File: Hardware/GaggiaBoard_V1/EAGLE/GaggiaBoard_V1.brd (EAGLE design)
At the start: 80 x 100 mm, 85 parts, among them IC1 LD117ADT33TR, J2 Vertical Qwiic Connector, J3 Vertical Qwiic Connector, J4 1X2-3.5MM, J5 1X2-3.5MM, K1 RELAY-SPDT-JZC-11F, K2 RELAY-SPDT-JZC-11F, K3 RELAY-SPDT-JZC-11F, Q1 600mA/40V, Q2 600mA/40V, Q3 600mA/40V, Q4 600mA/40V, Q5 600mA/40V, Q6 600mA/40V, Q7 2N7002D, Q8 600mA/40V, Q9 600mA/40V, U1 BLACKPILL, U2 MAX31855K, U3 MAX31855K, U4 MOC3021MDIL06O

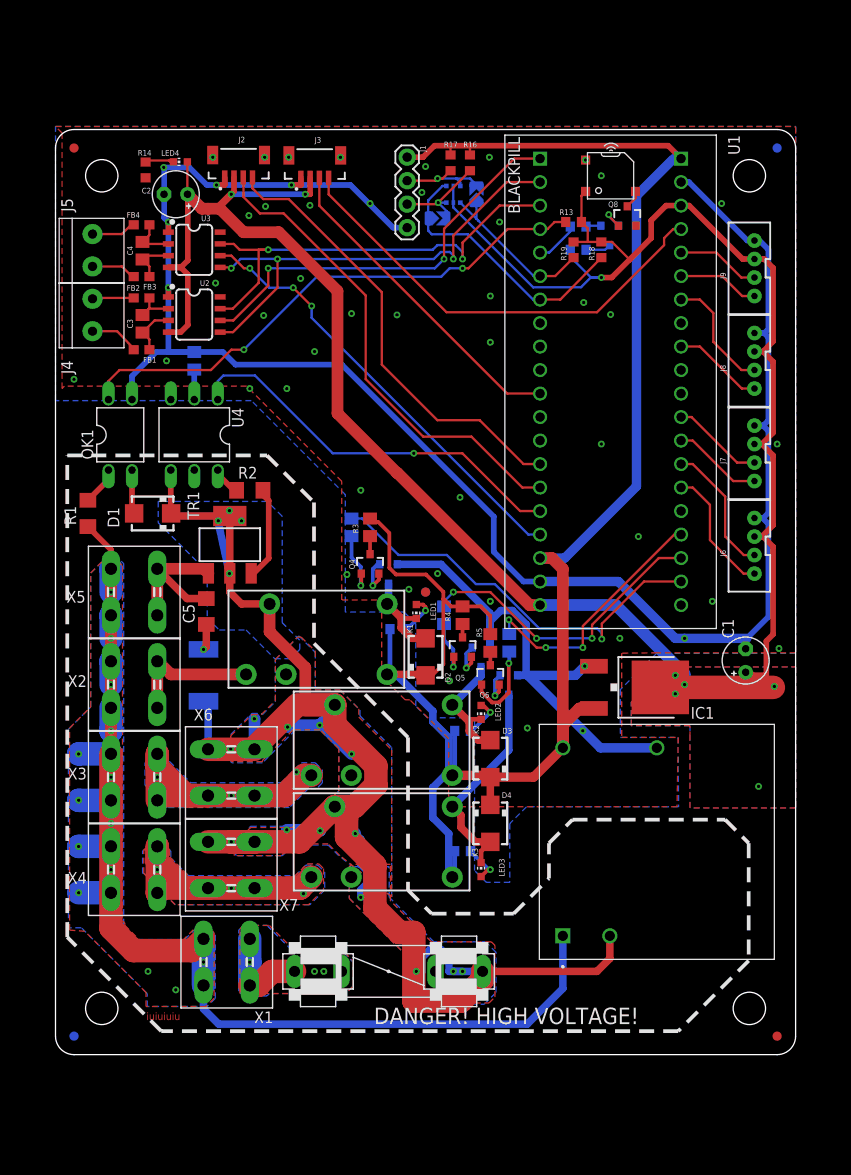
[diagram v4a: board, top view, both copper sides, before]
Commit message: PSU replaced
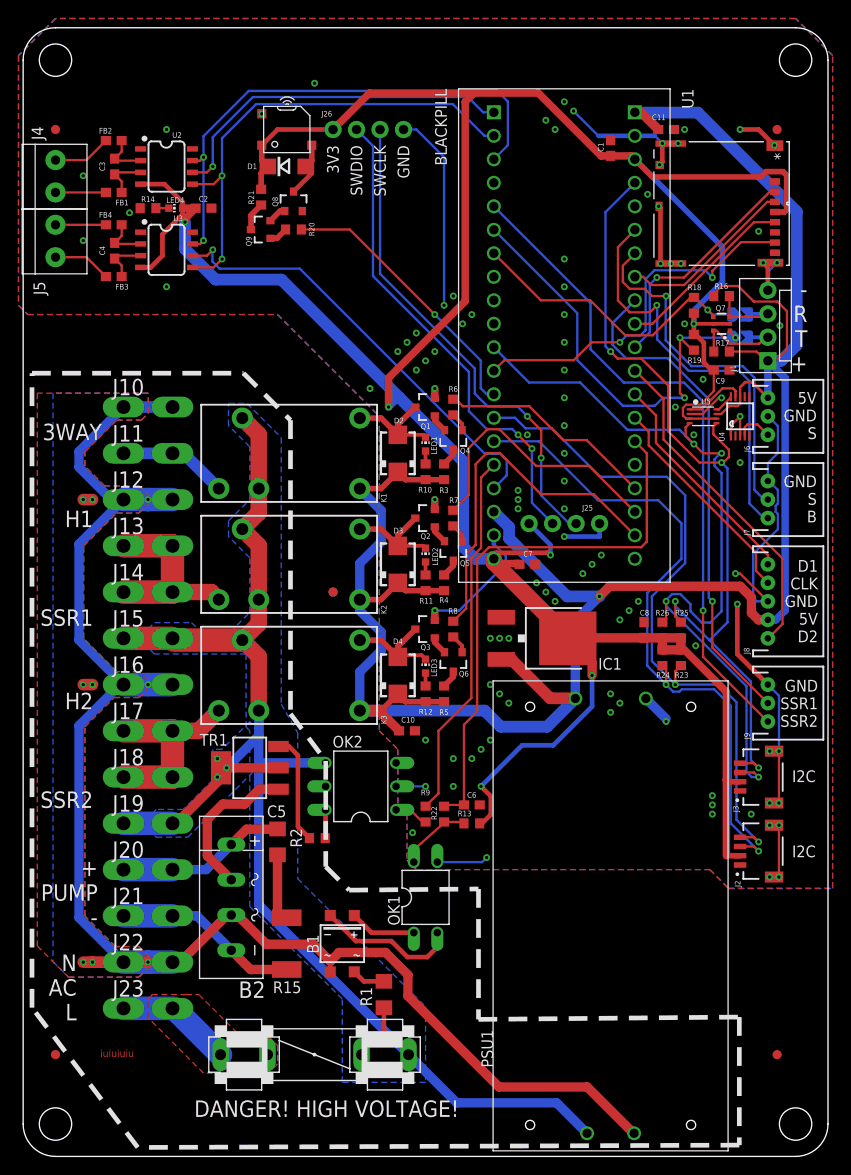
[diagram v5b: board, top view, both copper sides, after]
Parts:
- removed PS1: PSK-3D-5, PSK-3D-5:CONV_PSK-3D-5
- removed X1, X2, X3, X4, X5, X6, X7: (no value), con-rib:SH5-2
- added B1: MB6S, rectifier:SOIC-4
- added B2: RECTIFIER-2KBP, rectifier:2KBP
- added C10, C11, C6, C7, C8, C9: 10uF/16V, rcl:C0603
- added J10, J11, J12, J13, J14, J15, J16, J17, J18, J19, J20, J21, J22, J23: PIN262409-1, con-faston:62409-1
- added J24: 5033981892, discrete:503398-1892_MOL
- added J25, J26: (no value), SparkFun-Connectors:1X04_NO_SILK
- added OK2: MOC3021MDIL06O, discrete:DIL06O
- added PSU1: SM-PLG06-05, discrete:SM-PLG06
- added R22: 100, rcl:R0603
- added R23, R24, R25, R26: 10K, rcl:R0603
- added U5: (no value), adafruit:VFSOP-8
- C1, C2: device rcl:E2,5-5 -> rcl:C0603
- C3, C4: device rcl:C0805 -> rcl:C0603
- D1: value S1M -> 1N4007; device diode:SMA -> diode:DO214AC
- F1: value 30A -> 6A
- J1: device SparkFun-Connectors:1X04 -> SparkFun-Connectors:MOLEX-1X4
- J2, J3: value Vertical Qwiic Connector -> QWIIC_RIGHT_ANGLE; device SparkFun-Connectors:JST04_1MM_VERT -> SparkFun-Connectors:JST04_1MM_RA
- J6, J7, J9: device SparkFun-Connectors:JST-4-PTH-VERT -> SparkFun-Connectors:JST-3-PTH
- J8: device SparkFun-Connectors:JST-4-PTH-VERT -> SparkFun-Connectors:JST-5-PTH
- Q7: value 2N7002D -> (none)
- R10, R11, R12: value 330 -> 120
- R14: value 330 -> 51
- R2: device rcl:R1206 -> rcl:R0603
- R3, R4, R5, R6, R7, R8, R9: device rcl:R0805 -> rcl:R0603
- U4: value MOC3021MDIL06O -> (none); device discrete:DIL06O -> microbuilder:MSOP10
- moved J2 90.2 mm to (74.0, 22.0), turned to 90 degrees
- moved J3 78.8 mm to (74.0, 30.0), turned to 90 degrees
- moved R13 65.9 mm to (45.0, 25.0)
- moved R1 61.1 mm to (35.5, 6.50)
- moved OK1 59.9 mm to (40.0, 17.0)
- moved U4 59.0 mm to (74.0, 69.0), turned to 0 degrees
- moved C1 57.3 mm to (60.0, 98.0)
- moved R9 55.0 mm to (40.0, 26.0), flipped to the top
- moved J9 47.0 mm to (77.0, 38.0), turned to 270 degrees
- moved J1 44.8 mm to (77.0, 75.0), turned to 90 degrees
- moved D1 40.2 mm to (25.0, 96.0), turned to 0 degrees
- moved R2 38.3 mm to (28.3, 23.4), turned to 180 degrees
- moved Q9 37.7 mm to (22.2, 89.2), flipped to the top, turned to 90 degrees
- moved Q8 36.1 mm to (25.7, 92.2)
- moved R17 35.7 mm to (72.0, 76.0), turned to 0 degrees
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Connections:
- removed net PB15: OK1.4, R13.1, U1.P1$4
- removed net PB2: J9.2, U1.P2$5
- new net N$36: OK1.4, R13.1, R22.1
- new net N$37: B1.~2, R1.2
- new net N$38: U4.9, U5.P$1
- new net N$39: OK2.1, R9.2
- new net N$40: B2.AC2, TR1.1
- new net PB5: R20.1, U1.P1$13
- new net PRESSURE: J6.3, U4.4
- new net PUMP_N: B2.-, J21.A1, J21.A2, R15.1
- new net SPI1_MISO: J24.7, U1.P1$12
- new net SPI1_MOSI: J24.3, U1.P2$8
- new net SPI1_NSS: J24.2, U1.P2$11
- new net SPI1_SCK: J24.5, U1.P2$10
- new net SWCLK: J25.3, J26.3
- new net SWDIO: J25.2, J26.2
- net 3V3: now also C1.1, C2.1, C7.1, C8.1, C9.1, D1.C, J24.4, J25.1, J26.1, R23.1, R24.1, R25.1, R26.1, U5.P$3, U5.P$6; no longer C1.+, C2.+, J6.3, J7.3, J8.3, J9.3
- net 3WAY: now also J11.A1, J11.A2; no longer X2.1, X2.2
- net 5V: now also C10.1, C11.1, J6.1, J8.4, PSU1.VO+, U4.8, U5.P$7; no longer PS1.5
- net AC_N: now also B1.~1, B2.AC1, J10.A1, J10.A2, J12.A1, J12.A2, J16.A1, J16.A2, J22.A1, J22.A2, PSU1.AC_N; no longer PS1.1, R1.1, X1.3, X1.4, X2.3, X2.4, X3.3, X3.4, X4.3, X4.4, X5.3, X5.4
- net AC_P: now also J15.A1, J15.A2, J19.A1, J19.A2, K1.2, K2.2, K3.2, OK2.4, PSU1.AC_L, R1.1; no longer D1.C, PS1.2, R15.1, U4.4, X6.3, X6.4, X7.3, X7.4
- net GND: now also C1.2, C10.2, C11.2, C2.2, C6.2, C7.2, C8.2, C9.2, J24.6, J25.4, J26.4, J6.2, J7.1, J8.3, J9.1, OK2.2, PSU1.VO-, U4.1, U4.3, U4.5, U4.6, U4.7, U5.P$2; no longer C1.-, C2.-, J6.4, J7.4, J8.4, J9.4, PS1.4, R9.1
- net HEATER_1: now also J13.A1, J13.A2, J14.A1, J14.A2; no longer X3.1, X3.2, X6.1, X6.2
- net HEATER_2: now also J17.A1, J17.A2, J18.A1, J18.A2; no longer X4.1, X4.2, X7.1, X7.2
- net I2C1_SCL: now also R23.2
- net I2C1_SDA: now also R24.2
- net I2C2_SCL: now also R25.2, U5.P$5
- net I2C2_SDA: now also R26.2, U5.P$4
- net N$1: now also J23.A1, J23.A2; no longer X1.1, X1.2
- net N$2: now also B1.+; no longer R1.2
- net N$22: now also U4.10, U5.P$8; no longer R9.2, U4.2
- net N$30: now also D1.A
- net N$7: now also B1.-; no longer D1.A
- net N$8: now also OK2.6; no longer U4.6
- net PA0: now also C6.1, R22.2; no longer J6.1
- net PA1: now also J8.2; no longer J6.2
- net PA2: now also J8.1; no longer J7.1
- net PA3: now also J8.5; no longer J7.2
- net PA6: now also J9.2; no longer J8.1
- net PA8: now also J9.3; no longer R20.1
- net PB0: now also J7.2; no longer J8.2
- net PB1: now also J7.3; no longer J9.1
- net PB8: now also R9.1; no longer U4.1
- net PC13: now also R8.1; no longer R6.1
- net PC15: now also R6.1; no longer R8.1
- net PUMP_P: now also B2.+, J20.A1, J20.A2; no longer TR1.1, X5.1, X5.2
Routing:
- net GND: track 260.3 -> 152.9 mm, vias 51 -> 105
- net 3V3: track 257.8 -> 331.8 mm, vias 8 -> 6
- net PA8: track 4.73 -> 71.8 mm, vias 0 -> 1
- net PB15: track 58.5 -> 0.00 mm, vias 2 -> 0
- net SWCLK: track 0.00 -> 53.7 mm, vias 0 -> 2
- net SWDIO: track 0.00 -> 53.0 mm, vias 0 -> 2
- net I2C2_SDA: track 35.3 -> 86.8 mm, vias 0 -> 4
- net 5V: track 205.8 -> 255.0 mm, vias 0 -> 1
- net AC_P: track 204.6 -> 158.7 mm, vias 17 -> 3
- net PA0: track 14.0 -> 59.9 mm
- net PA6: track 9.81 -> 54.1 mm, vias 0 -> 1
- net I2C2_SCL: track 49.3 -> 91.9 mm, vias 0 -> 4
- net SPI1_MISO: track 0.00 -> 40.5 mm, vias 0 -> 2
- net PB1: track 8.82 -> 44.9 mm, vias 0 -> 1
- net UART1_TX: track 18.0 -> 48.1 mm, vias 0 -> 3
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- removed copper zone on layer 1, net 3V3
- removed copper zone on layer 16, net 3V3
- removed copper zone on layer 1, net AC_P
- removed copper zone on layer 16, net HEATER_1
- removed copper zone on layer 1, net HEATER_2
- removed copper zone on layer 16, net HEATER_2
- removed copper zone on layer 16, net N$1
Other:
- board size 80 x 100 mm -> 87 x 122 mm
- board text added: "+ PUMP -"
- board text added: "- R T +"
- board text added: "3V3 SWDIO SWCLK GND"
- board text added: "3WAY"
- board text added: "5V GND S"
- board text added: "D1 CLK GND 5V D2"
- board text added: "GND S B"
- board text added: "GND SSR1 SSR2"
- board text added: "H1 SSR1"
- board text added: "H2 SSR2"
- board text added: "I2C"
- board text added: "N AC L"

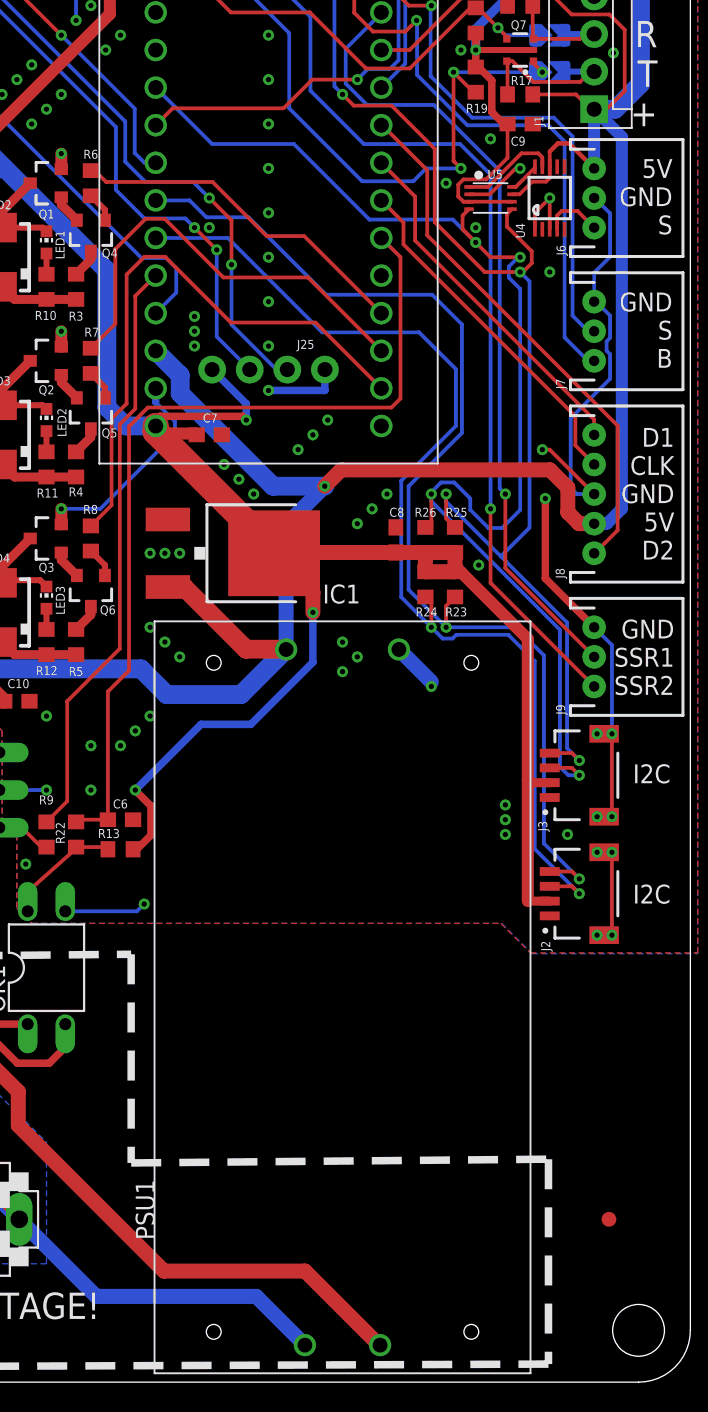
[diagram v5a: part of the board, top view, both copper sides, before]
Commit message: MEAN WELL PSU option, discrete level shifters
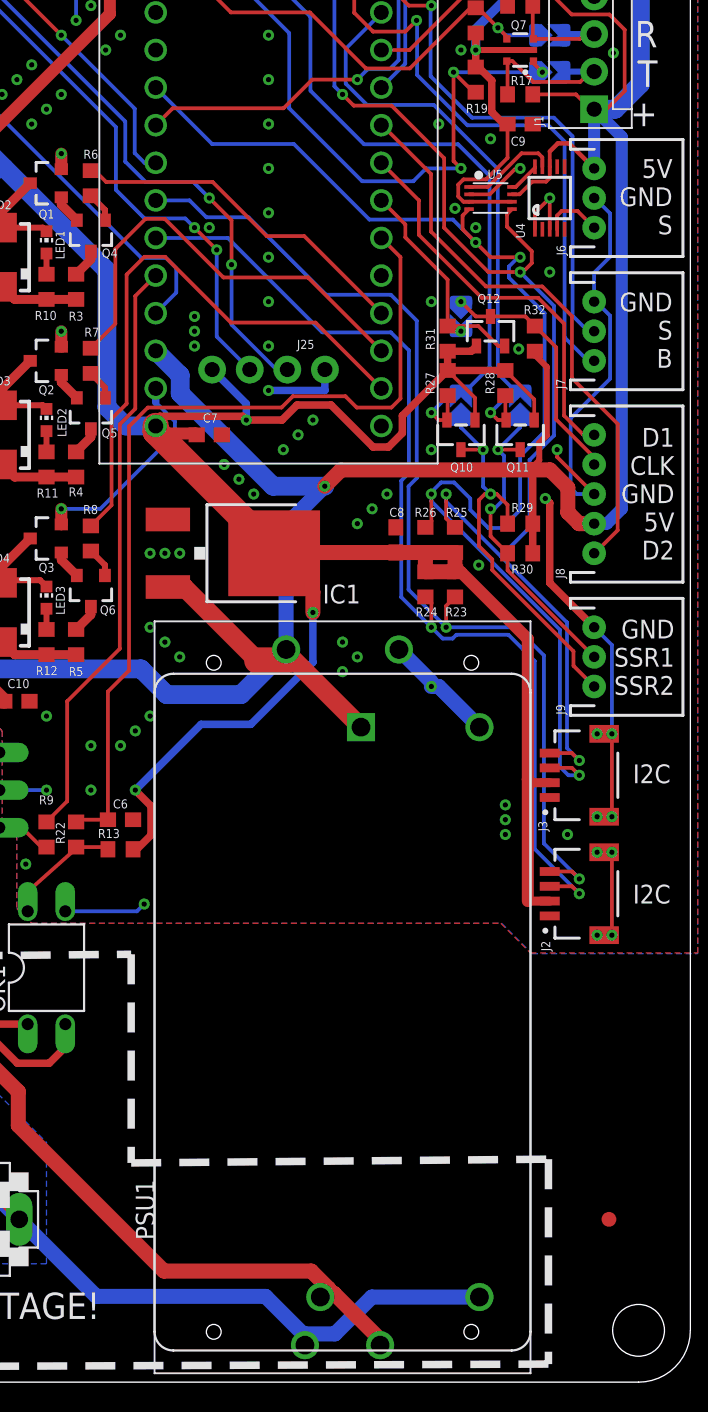
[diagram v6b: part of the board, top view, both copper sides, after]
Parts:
- added PSU2: IRM-10-5, discrete:IRM-10
- added Q10, Q11, Q12: (no value), microbuilder:SOT23-R
- added R27, R28, R29, R30, R31, R32: 10K, rcl:R0603
- added SJ3, SJ4, SJ5: (no value), microbuilder:SOLDERJUMPER_ARROW_NOPASTE
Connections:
- new net N$41: J9.2, Q11.3, R30.2, SJ4.1
- new net N$42: J9.3, Q10.3, R29.2, SJ3.1
- new net N$43: J8.2, Q12.3, R32.1, SJ5.1
- net 3V3: now also Q10.1, Q11.1, Q12.1, R27.1, R28.1, R31.2
- net 5V: now also PSU2.+V, R29.1, R30.1, R32.2
- net AC_N: now also PSU2.AC/N
- net AC_P: now also PSU2.AC/L
- net GND: now also PSU2.-V
- net PA1: now also Q12.2, R31.1, SJ5.2; no longer J8.2
- net PA6: now also Q11.2, R28.2, SJ4.2; no longer J9.2
- net PA8: now also Q10.2, R27.2, SJ3.2; no longer J9.3
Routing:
- net 3V3: track 331.8 -> 365.4 mm
- net N$42: track 0.00 -> 26.8 mm, vias 0 -> 2
- net 5V: track 255.0 -> 278.0 mm
- net N$41: track 0.00 -> 21.7 mm, vias 0 -> 2
- net N$43: track 0.00 -> 16.7 mm, vias 0 -> 1
- net PA8: track 71.8 -> 55.3 mm
- net PA6: track 54.1 -> 39.8 mm
- net AC_P: track 158.7 -> 172.6 mm
- net PA1: track 23.8 -> 15.6 mm, vias 0 -> 1
- net I2C1_SCL: track 75.1 -> 71.0 mm
- net I2C1_SDA: track 73.3 -> 69.5 mm
- net GND: track 152.9 -> 156.4 mm, vias 105 -> 109
- net PA2: track 24.3 -> 27.0 mm
- net PA3: track 36.2 -> 38.5 mm
- net AC_N: track 168.2 -> 169.8 mm
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
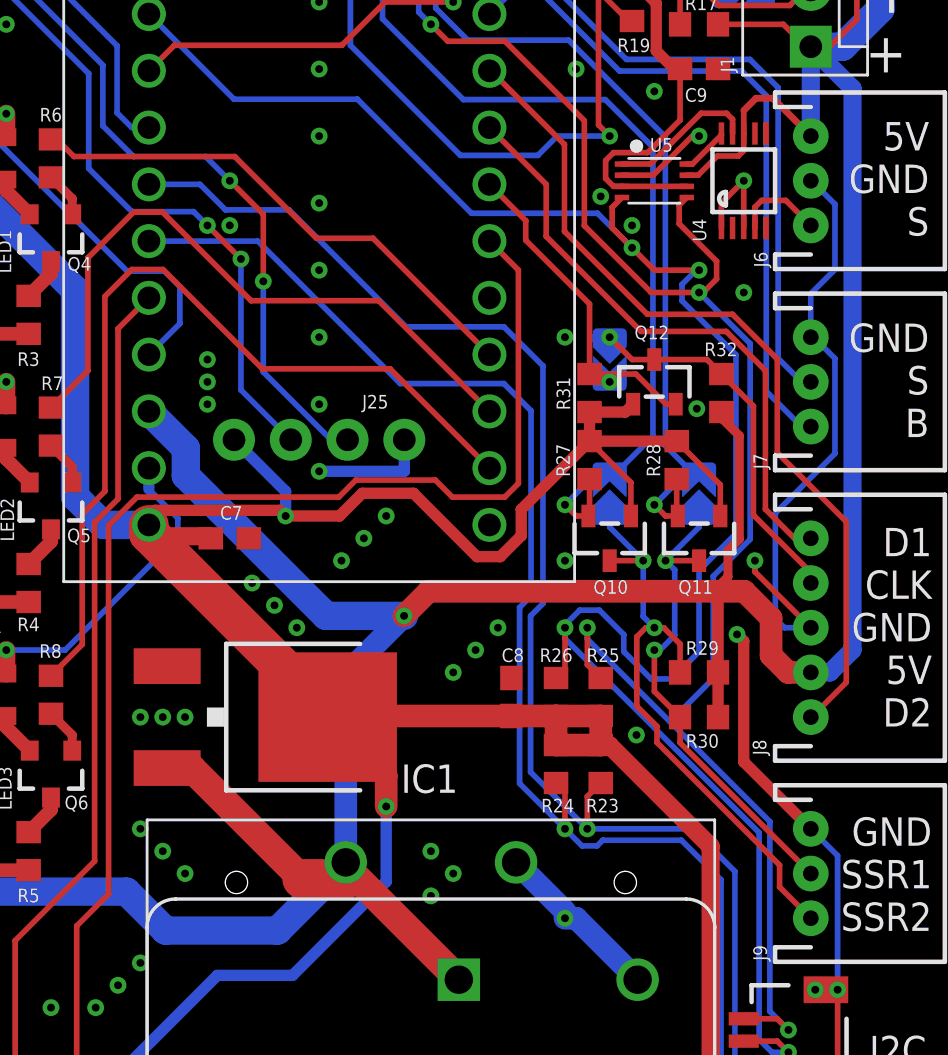
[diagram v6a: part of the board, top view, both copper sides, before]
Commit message: TXU0102 level shifter for SSRs
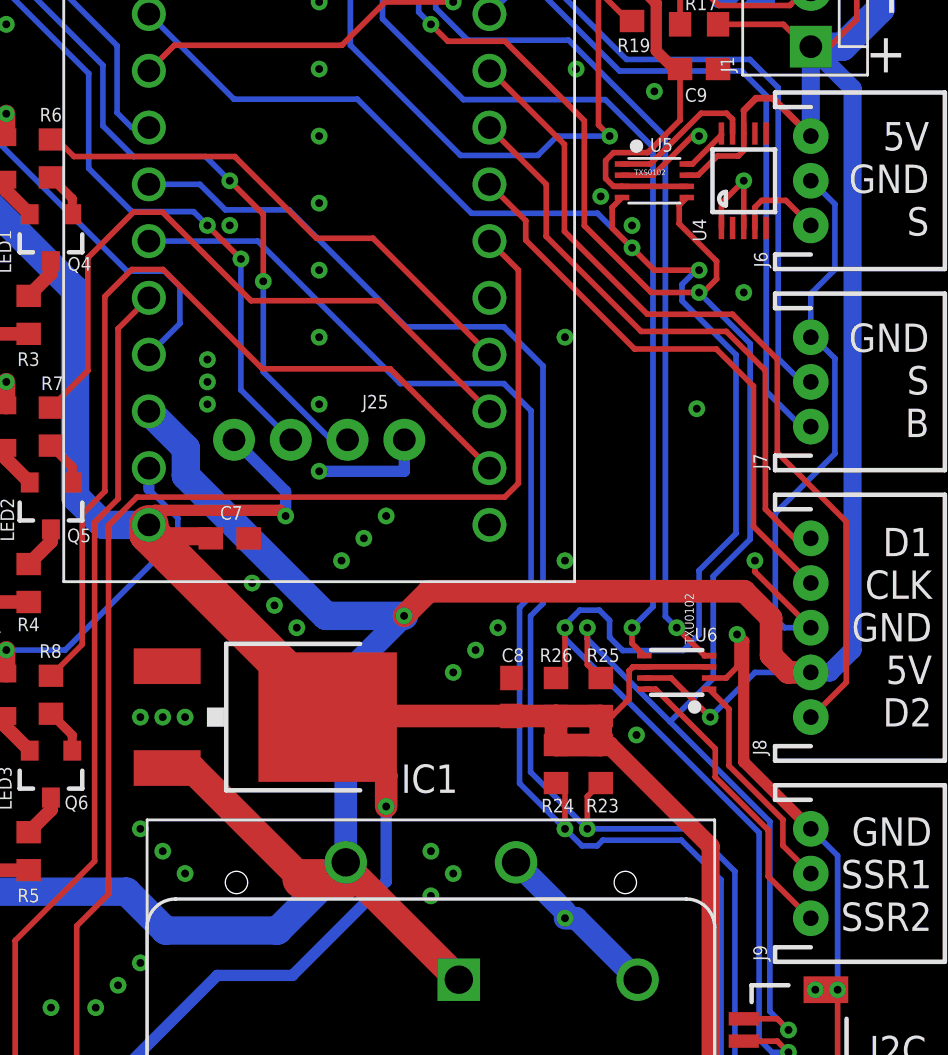
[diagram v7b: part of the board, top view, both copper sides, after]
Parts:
- removed Q10, Q11, Q12: (no value), microbuilder:SOT23-R
- removed R27, R28, R29, R30, R31, R32: 10K, rcl:R0603
- removed SJ3, SJ4, SJ5: (no value), microbuilder:SOLDERJUMPER_ARROW_NOPASTE
- added U6: TXU0102, microbuilder:VFSOP-8
- U5: value (none) -> TXS0102
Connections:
- removed net N$43: J8.2, Q12.3, R32.1, SJ5.1
- net 3V3: now also U6.3, U6.6; no longer Q10.1, Q11.1, Q12.1, R27.1, R28.1, R31.2
- net 5V: now also U6.7; no longer R29.1, R30.1, R32.2
- net GND: now also U6.2
- net N$41: now also J9.3, U6.8; no longer J9.2, Q11.3, R30.2, SJ4.1
- net N$42: now also J9.2, U6.1; no longer J9.3, Q10.3, R29.2, SJ3.1
- net PA1: now also J8.2; no longer Q12.2, R31.1, SJ5.2
- net PA6: now also U6.4; no longer Q11.2, R28.2, SJ4.2
- net PA8: now also U6.5; no longer Q10.2, R27.2, SJ3.2
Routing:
- net 3V3: track 365.4 -> 338.3 mm
- net N$43: track 16.7 -> 0.00 mm, vias 1 -> 0
- net N$42: track 26.8 -> 10.1 mm, vias 2 -> 0
- net PA1: track 15.6 -> 26.0 mm, vias 1 -> 0
- net N$41: track 21.7 -> 13.7 mm, vias 2 -> 0
- net 5V: track 278.0 -> 272.5 mm, vias 1 -> 2
- net GND: track 156.4 -> 159.3 mm
- net PA6: track 39.8 -> 42.6 mm
- net PA8: track 55.3 -> 57.6 mm
- net I2C2_SDA: track 88.1 -> 86.6 mm
- net PA0: track 60.5 -> 59.9 mm
